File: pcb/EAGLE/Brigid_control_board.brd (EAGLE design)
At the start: 53.3 x 53.3 mm, 33 parts, among them J1 ARDUINO_R3_SHIELD, P1 Molex Mini-Fit Jr., P2 Molex Mini-Fit Jr., P3 Molex Mini-Fit Jr., P4 Molex Mini-Fit Jr., P5 Molex Mini-Fit Jr., P6 Molex Mini-Fit Jr., P7 Molex Mini-Fit Jr., Q1 T460, Q2 T460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

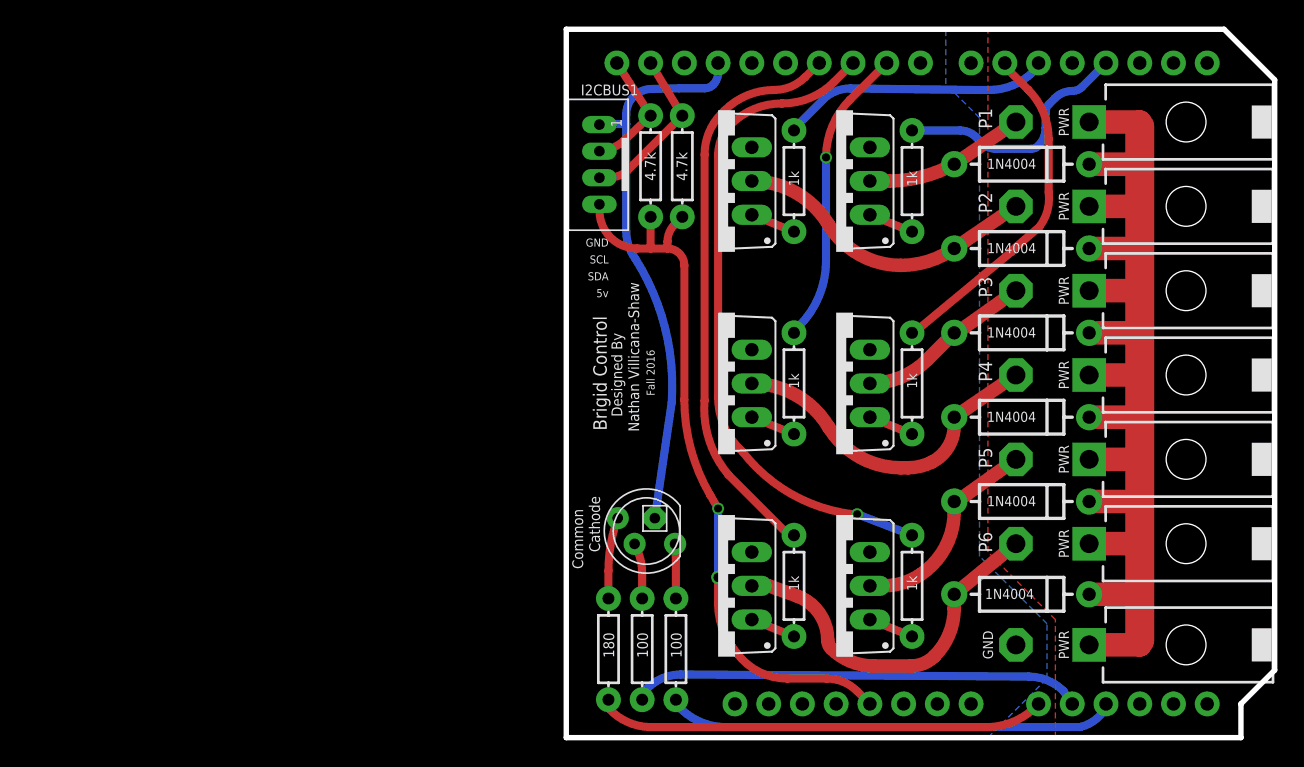
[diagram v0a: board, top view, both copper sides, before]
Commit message: modified board to be othermill friendly
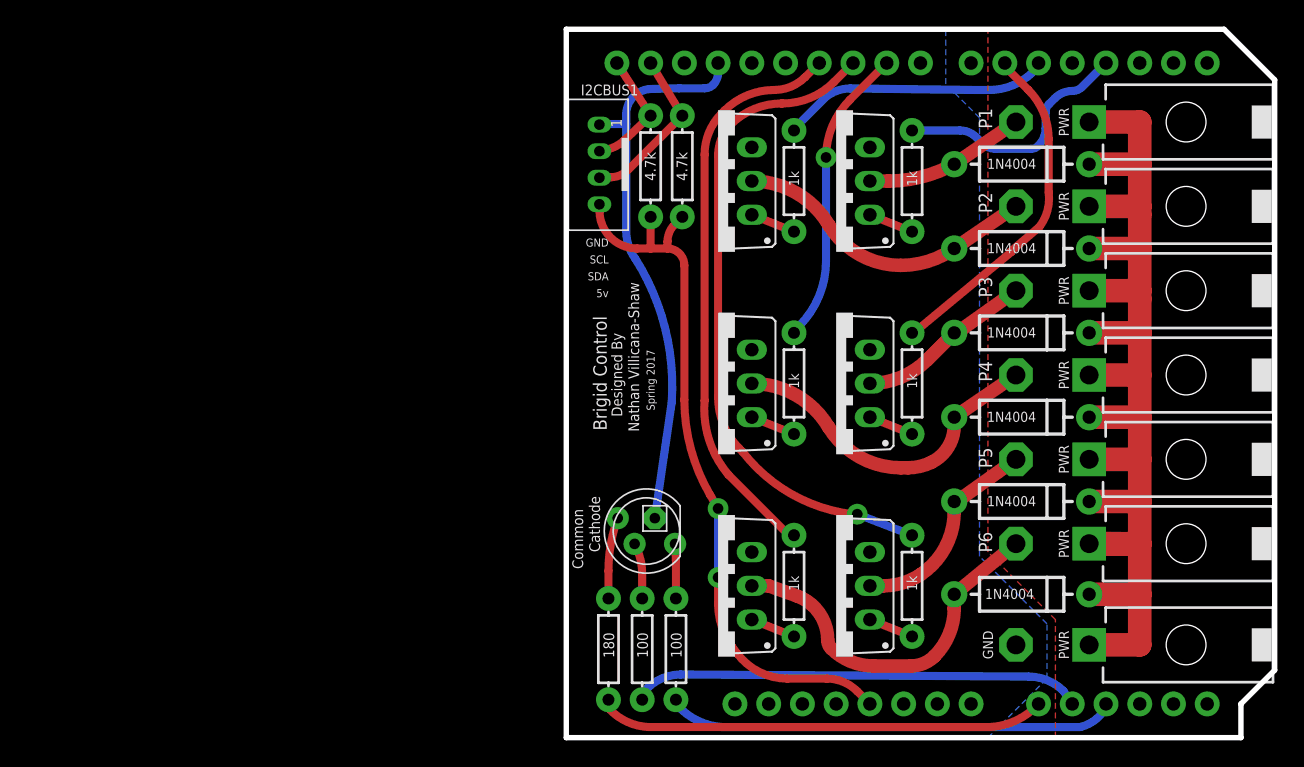
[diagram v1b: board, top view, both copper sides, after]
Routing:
- net N$6: track 38.7 -> 0.00 mm
- net PWR: track 94.0 -> 92.7 mm
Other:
- board text added: "Spring 2017"
- board text removed: "Fall 2016"

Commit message: added firmware for DC_Motors
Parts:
- added EXT-PWR, I2C-PWR-SEL: (no value), SparkFun-Electromechanical:SWITCH-SPDT_KIT
- renumbered P7 to POWER_IN, U$1 to RGB-STATUS-LED
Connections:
- net N$20 renamed A-GND
- new net 3.3V: I2C-PWR-SEL.3, J1.3.3V
- new net 5V: I2C-PWR-SEL.1, I2CBUS1.P4, J1.5V
- new net I2C-PWR: I2C-PWR-SEL.2, R10.P$1, R11.P$1
- new net VIN: EXT-PWR.1, J1.VIN
- net N$17: now also EXT-PWR.3; no longer I2CBUS1.P4, J1.5V, R10.P$1, R11.P$1
- net PWR: now also EXT-PWR.2
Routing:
- net N$17: track 54.7 -> 0.00 mm, vias 2 -> 0
- net I2C-PWR: track 0.00 -> 52.0 mm, vias 0 -> 2
- net A-GND: track 42.1 -> 32.6 mm
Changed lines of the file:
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@@
 <attribute name="VALUE" x="16.764" y="12.192" size="0.762" layer="21" font="vector" ratio="15" rot="R270"/>
 </element>
-<element name="P7" library="con-molex-mini-fit" package="39-30-?02?" value="Molex Mini-Fit Jr." x="39.37" y="6.985" smashed="yes" rot="R90"/>
-<element name="U$1" library="adafruit" package="LED5MMRGB" value="RGB LED" x="6.0325" y="15.5575" smashed="yes" rot="R180"/>
+<element name="POWER_IN" library="con-molex-mini-fit" package="39-30-?02?" value="Molex Mini-Fit Jr." x="39.37" y="6.985" smashed="yes" rot="R90"/>
+<element name="RGB-STATUS-LED" library="adafruit" package="LED5MMRGB" value="RGB LED" x="6.0325" y="15.5575" smashed="yes" rot="R180"/>
 <element name="R1" library="SparkFun-Passives" package="AXIAL-0.3EZ" value="100" x="8.255" y="6.6675" smashed="yes" rot="R270">
 <attribute name="VALUE" x="7.874" y="7.921625" size="0.8128" layer="21" font="vector" ratio="15" rot="R270"/>
@@
 <element name="R11" library="SparkFun-Passives" package="AXIAL-0.3EZ" value="4.7k" x="8.734425" y="43.024425" smashed="yes" rot="R90">
 <attribute name="VALUE" x="9.115425" y="41.925875" size="0.8128" layer="21" font="vector" ratio="15" rot="R90"/>
+</element>
+<element name="I2C-PWR-SEL" library="SparkFun-Electromechanical" package="SWITCH-SPDT_KIT" value="" x="-17.78" y="6.35">
+<attribute name="PROD_ID" value="SWCH-08261" x="-17.78" y="6.35" size="1.778" layer="27" display="off"/>
+</element>
+<element name="EXT-PWR" library="SparkFun-Electromechanical" package="SWITCH-SPDT_KIT" value="" x="-36.83" y="6.35">
+<attribute name="PROD_ID" value="SWCH-08261" x="-36.83" y="6.35" size="1.778" layer="27" display="off"/>
 </element>
 </elements>
@@
 </signal>
 <signal name="GND">
-<contactref element="P7" pad="2"/>
+<contactref element="POWER_IN" pad="2"/>
 <polygon width="0.6096" layer="16">
 <vertex x="0" y="53.34"/>
@@
 <contactref element="P6" pad="1"/>
 <contactref element="D7" pad="C"/>
-<contactref element="P7" pad="1"/>
+<contactref element="POWER_IN" pad="1"/>
 <wire x1="39.37" y1="6.985" x2="43.18" y2="6.985" width="1.778" layer="1"/>
 <wire x1="43.18" y1="6.985" x2="43.18" y2="10.795" width="1.778" layer="1"/>
@@
 <wire x1="43.18" y1="33.655" x2="43.18" y2="36.83" width="1.778" layer="1"/>
 <wire x1="43.18" y1="40.005" x2="43.18" y2="43.18" width="1.778" layer="1"/>
+<contactref element="EXT-PWR" pad="2"/>
 <wire x1="39.37" y1="30.48" x2="39.37" y2="27.305" width="0" layer="19" extent="1-1"/>
+<wire x1="-36.83" y1="6.35" x2="39.37" y2="6.985" width="0" layer="19" extent="1-1"/>
 </signal>
 <signal name="D3">
@@
 <signal name="N$5">
 <contactref element="R9" pad="P$1"/>
-<contactref element="U$1" pad="4"/>
+<contactref element="RGB-STATUS-LED" pad="4"/>
 <wire x1="3.8735" y1="16.5259" x2="3.175" y2="12.56104375" width="0.6096" layer="1" curve="19.982867"/>
 <wire x1="3.175" y1="12.56104375" x2="3.175" y2="10.4775" width="0.6096" layer="1"/>
@@
 <signal name="N$7">
 <contactref element="R1" pad="P$1"/>
-<contactref element="U$1" pad="1"/>
+<contactref element="RGB-STATUS-LED" pad="1"/>
 <wire x1="8.1915" y1="14.5891" x2="8.255" y2="13.335" width="0.6096" layer="1"/>
 <wire x1="8.255" y1="13.335" x2="8.255" y2="10.4775" width="0.6096" layer="1"/>
@@
 <signal name="N$8">
 <contactref element="R8" pad="P$1"/>
-<contactref element="U$1" pad="3"/>
+<contactref element="RGB-STATUS-LED" pad="3"/>
 <wire x1="5.1435" y1="14.5891" x2="5.310746875" y2="14.22209375" width="0.6096" layer="1"/>
 <wire x1="5.310746875" y1="14.22209375" x2="5.715" y2="12.360140625" width="0.6096" layer="1" curve="-24.499002"/>
 <wire x1="5.715" y1="12.360140625" x2="5.715" y2="10.4775" width="0.6096" layer="1"/>
-</signal>
-<signal name="N$20">
-<contactref element="U$1" pad="2"/>
-<contactref element="J1" pad="GND@2"/>
-<contactref element="I2CBUS1" pad="P1"/>
-<wire x1="11.43" y1="50.8" x2="11.43" y2="50.05605" width="0.6096" layer="16"/>
-<wire x1="11.43" y1="50.05605" x2="11.058025" y2="49.158025" width="0.6096" layer="16" curve="-45"/>
-<wire x1="11.058025" y1="49.158025" x2="10.423025" y2="48.895" width="0.6096" layer="16" curve="-45"/>
-<wire x1="10.423025" y1="48.895" x2="8.4963" y2="48.895" width="0.6096" layer="16"/>
-<wire x1="8.4963" y1="48.895" x2="6.381815625" y2="48.844453125" width="0.6096" layer="16"/>
-<wire x1="6.381815625" y1="48.844453125" x2="4.511675" y2="46.929078125" width="0.6096" layer="16" curve="88.632509"/>
-<wire x1="4.511675" y1="46.929078125" x2="4.511675" y2="46.205775" width="0.6096" layer="16"/>
-<wire x1="4.511675" y1="46.205775" x2="4.511675" y2="38.156615625" width="0.6096" layer="16"/>
-<wire x1="4.511675" y1="38.156615625" x2="5.197578125" y2="36.06488125" width="0.6096" layer="16" curve="36.309795"/>
-<wire x1="5.197578125" y1="36.06488125" x2="7.9375" y2="25.232259375" width="0.6096" layer="16" curve="-36.310237"/>
-<wire x1="7.9375" y1="25.232259375" x2="6.6675" y2="16.5259" width="0.6096" layer="16"/>
-<wire x1="2.4925" y1="46.16" x2="2.538275" y2="46.205775" width="0.8128" layer="16"/>
-<wire x1="2.538275" y1="46.205775" x2="4.511675" y2="46.205775" width="0.6096" layer="16"/>
 </signal>
 <signal name="SDA">
@@
 <wire x1="8.255" y1="2.54" x2="8.255" y2="2.8575" width="0.6096" layer="16"/>
 </signal>
-<signal name="N$17">
-<contactref element="R11" pad="P$1"/>
+<signal name="I2C-PWR">
 <contactref element="R10" pad="P$1"/>
-<contactref element="I2CBUS1" pad="P4"/>
-<contactref element="J1" pad="5V"/>
-<wire x1="22.86" y1="2.54" x2="21.903353125" y2="3.496646875" width="0.6096" layer="1"/>
 <wire x1="21.903353125" y1="3.496646875" x2="19.613828125" y2="4.445" width="0.6096" layer="1" curve="45.000055"/>
 <wire x1="19.613828125" y1="4.445" x2="16.6474875" y2="4.445" width="0.6096" layer="1"/>
@@
 <wire x1="6.35" y1="36.83" x2="5.3395875" y2="36.83" width="0.6096" layer="1"/>
 <wire x1="5.3395875" y1="36.83" x2="2.50006875" y2="39.629390625" width="0.6096" layer="1" curve="-89.184549"/>
-<wire x1="2.50006875" y1="39.629390625" x2="2.4925" y2="40.16" width="0.6096" layer="1"/>
 <wire x1="6.35" y1="39.214425" x2="6.35" y2="36.83" width="0.6096" layer="1"/>
-<wire x1="8.734425" y1="39.214425" x2="8.14605" y2="38.62605" width="0.6096" layer="1"/>
 <wire x1="8.14605" y1="38.62605" x2="7.62" y2="37.356053125" width="0.6096" layer="1" curve="44.9999"/>
 <wire x1="7.62" y1="37.356053125" x2="7.62" y2="36.83" width="0.6096" layer="1"/>
+<contactref element="R11" pad="P$1"/>
+<contactref element="I2C-PWR-SEL" pad="2"/>
+<wire x1="8.14605" y1="38.62605" x2="8.734425" y2="39.214425" width="0" layer="19" extent="1-1"/>
+<wire x1="-17.78" y1="6.35" x2="11.43" y2="10.063478125" width="0" layer="19" extent="1-1"/>
+</signal>
+<signal name="A-GND">
+<contactref element="RGB-STATUS-LED" pad="2"/>
+<contactref element="J1" pad="GND@2"/>
+<contactref element="I2CBUS1" pad="P1"/>
+<wire x1="11.43" y1="50.05605" x2="11.058025" y2="49.158025" width="0.6096" layer="16" curve="-45"/>
+<wire x1="11.058025" y1="49.158025" x2="10.423025" y2="48.895" width="0.6096" layer="16" curve="-45"/>
+<wire x1="10.423025" y1="48.895" x2="8.4963" y2="48.895" width="0.6096" layer="16"/>
+<wire x1="8.4963" y1="48.895" x2="6.381815625" y2="48.844453125" width="0.6096" layer="16"/>
+<wire x1="6.381815625" y1="48.844453125" x2="4.511675" y2="46.929078125" width="0.6096" layer="16" curve="88.632509"/>
+<wire x1="4.511675" y1="46.929078125" x2="4.511675" y2="46.205775" width="0.6096" layer="16"/>
+<wire x1="4.511675" y1="46.205775" x2="4.511675" y2="38.156615625" width="0.6096" layer="16"/>
+<wire x1="4.511675" y1="38.156615625" x2="5.197578125" y2="36.06488125" width="0.6096" layer="16" curve="36.309795"/>
+<wire x1="5.197578125" y1="36.06488125" x2="7.9375" y2="25.232259375" width="0.6096" layer="16" curve="-36.310237"/>
+<wire x1="2.4925" y1="46.16" x2="2.538275" y2="46.205775" width="0.8128" layer="16"/>
+<wire x1="2.538275" y1="46.205775" x2="4.511675" y2="46.205775" width="0.6096" layer="16"/>
+<wire x1="11.43" y1="50.05605" x2="11.43" y2="50.8" width="0" layer="19" extent="16-16"/>
+<wire x1="6.6675" y1="16.5259" x2="7.9375" y2="25.232259375" width="0" layer="19" extent="16-16"/>
+</signal>
+<signal name="5V">
+<contactref element="I2CBUS1" pad="P4"/>
+<contactref element="J1" pad="5V"/>
+<contactref element="I2C-PWR-SEL" pad="1"/>
+<wire x1="-17.78" y1="9.0678" x2="2.4925" y2="40.16" width="0" layer="19" extent="1-1"/>
+<wire x1="22.86" y1="2.54" x2="-17.78" y2="9.0678" width="0" layer="19" extent="1-1"/>
+</signal>
+<signal name="3.3V">
+<contactref element="I2C-PWR-SEL" pad="3"/>
+<contactref element="J1" pad="3.3V"/>
+<wire x1="-17.78" y1="3.6322" x2="20.32" y2="2.54" width="0" layer="19" extent="1-1"/>
+</signal>
+<signal name="VIN">
+<contactref element="EXT-PWR" pad="1"/>
+<contactref element="J1" pad="VIN"/>
+<wire x1="-36.83" y1="9.0678" x2="30.48" y2="2.54" width="0" layer="19" extent="1-1"/>
+</signal>
+<signal name="N$17">
+<contactref element="EXT-PWR" pad="3"/>
 </signal>
 </signals>

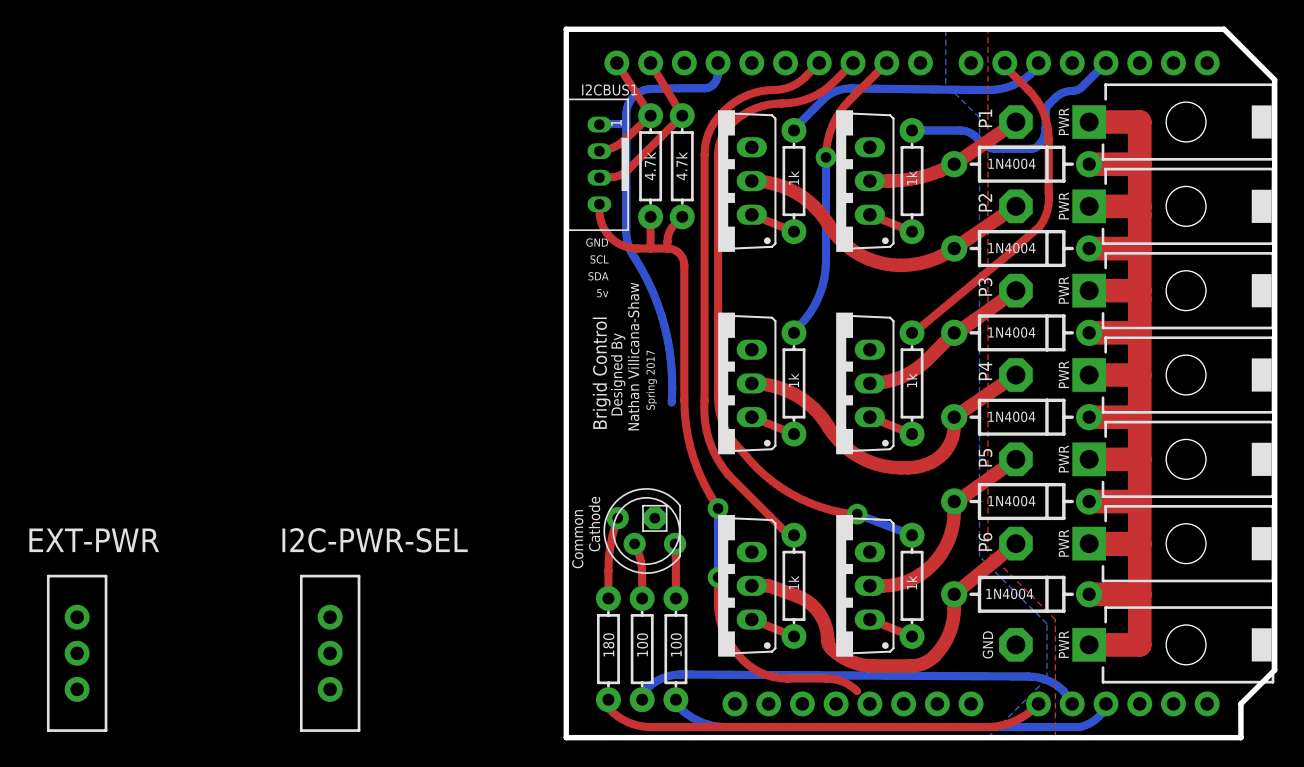
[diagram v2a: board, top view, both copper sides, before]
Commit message: updated brigid board, removed switched that were not needed
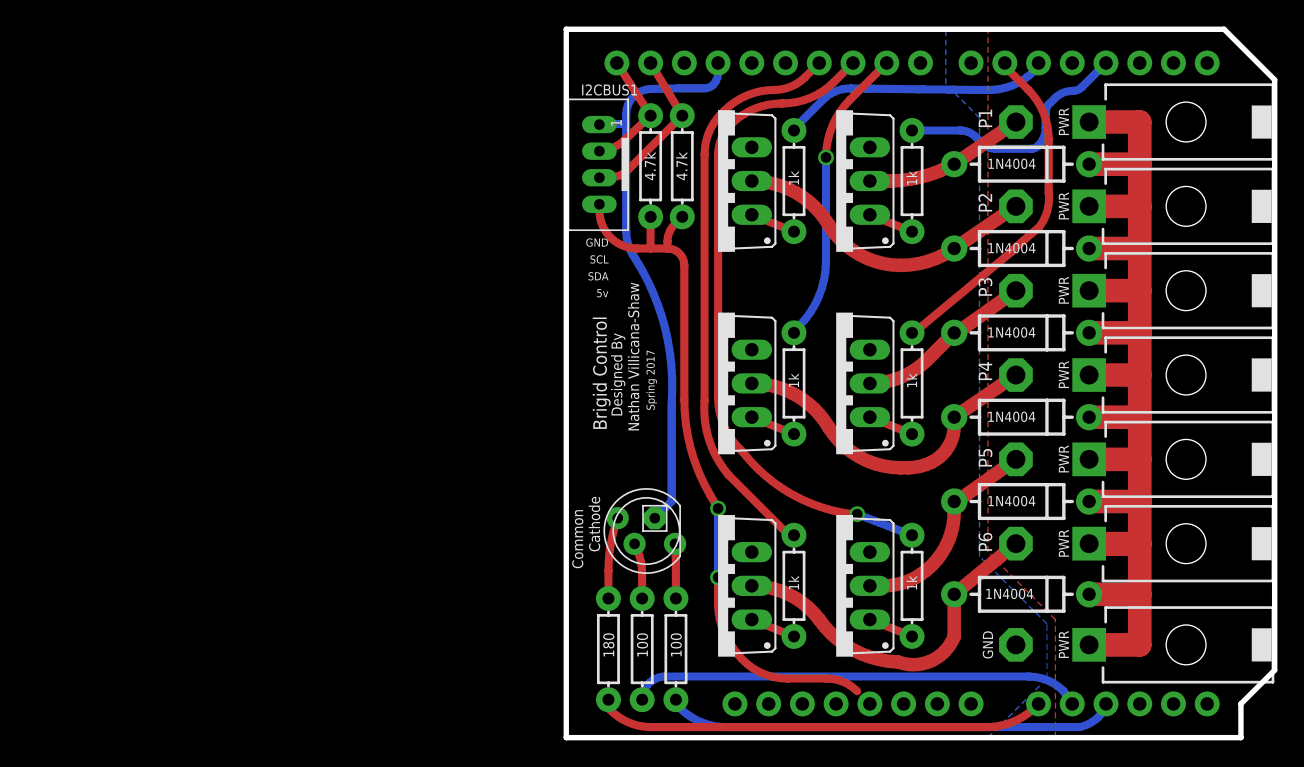
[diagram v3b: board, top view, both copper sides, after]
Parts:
- removed EXT-PWR, I2C-PWR-SEL: (no value), SparkFun-Electromechanical:SWITCH-SPDT_KIT
- added FRAME1: FRAME-LETTER, SparkFun-Aesthetics:CREATIVE_COMMONS
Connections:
- removed net I2C-PWR: I2C-PWR-SEL.2, R10.P$1, R11.P$1
- removed net N$17: EXT-PWR.3
- net 3.3V: no longer I2C-PWR-SEL.3
- net 5V: now also R10.P$1, R11.P$1; no longer I2C-PWR-SEL.1
- net PWR: no longer EXT-PWR.2
- net VIN: no longer EXT-PWR.1
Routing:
- net I2C-PWR: track 52.0 -> 0.00 mm, vias 2 -> 0
- net 5V: track 0.00 -> 52.0 mm, vias 0 -> 2
- net A-GND: track 32.6 -> 41.8 mm
- net N$22: track 27.4 -> 26.2 mm
